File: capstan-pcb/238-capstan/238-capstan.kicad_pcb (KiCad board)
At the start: 2 copper layers, 58 x 67 mm, 53 parts, among them CN1 CN1, IC1 BA6303F, IC2 4013, IC3 BA6411, J1 0, J2 0

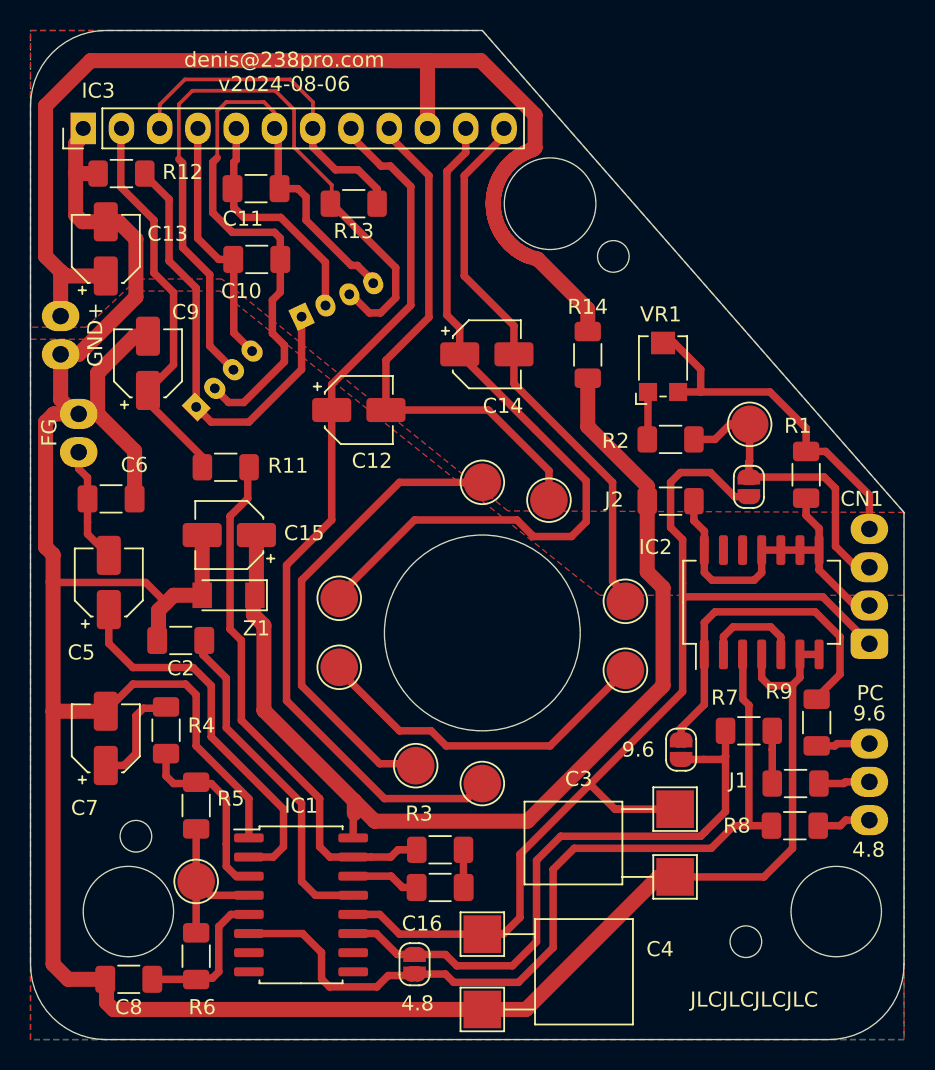
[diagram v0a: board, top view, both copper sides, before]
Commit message: Capstan PCB fix mouting hole position; larger pads for VR1; routing adjustments
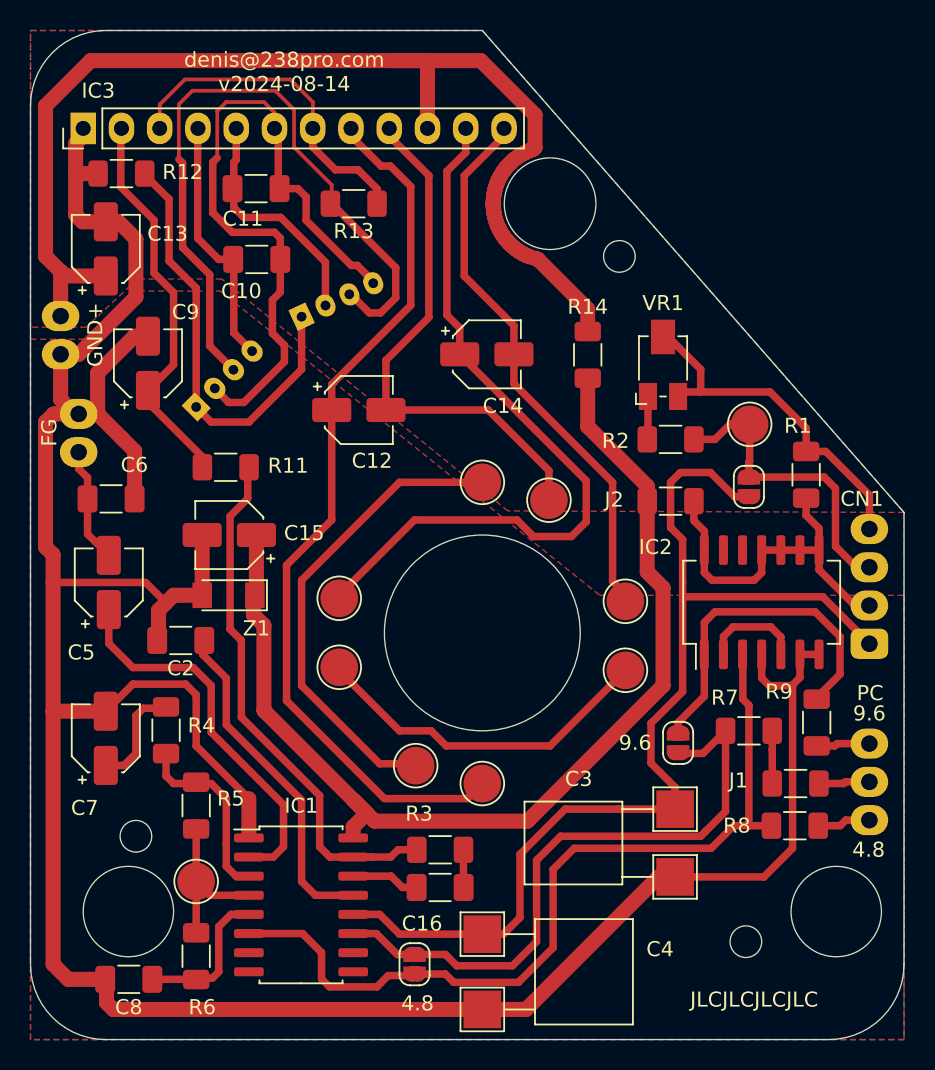
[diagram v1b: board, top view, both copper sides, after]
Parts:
- moved JP2 0.49 mm to (161.0, 97.3)
- moved H2 0.40 mm to (157.1, 65.0)
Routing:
- net Net-(C3-Pad2): track 72.0 -> 71.3 mm
- net Net-(IC1-Pad11): track 41.4 -> 42.0 mm
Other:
- board text added: "denis@238pro.com v2024-08-14"
- board text removed: "denis@238pro.com v2024-08-06"

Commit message: Capstan PCB gerbers v2024-08-15, minor tweaks, sent to fab
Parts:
- moved R11 1.26 mm to (129.7, 79.0)
- moved R14 0.96 mm to (155.0, 72.5)
- moved CN1 0.71 mm to (174.2, 91.2)
- moved IC2 0.70 mm to (165.8, 88.0)
- moved PC1 0.50 mm to (174.2, 97.3)
- moved H2 0.10 mm to (157.0, 65.0)
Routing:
- net +9V: track 70.8 -> 69.6 mm
- net Net-(CN1-Pad3): track 20.4 -> 21.6 mm
- net Net-(CN1-Pad2): track 24.0 -> 25.0 mm
- net Net-(IC2-Pad1): track 22.7 -> 21.7 mm
- net Net-(CN1-Pad4): track 23.4 -> 24.3 mm
- net Net-(C3-Pad2): track 71.3 -> 72.0 mm
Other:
- board text added: "1"
- board text added: "2"
- board text added: "3"
- board text added: "4"
- board text added: "denis@238pro.com v2024-08-15"
- board text removed: "denis@238pro.com v2024-08-14"

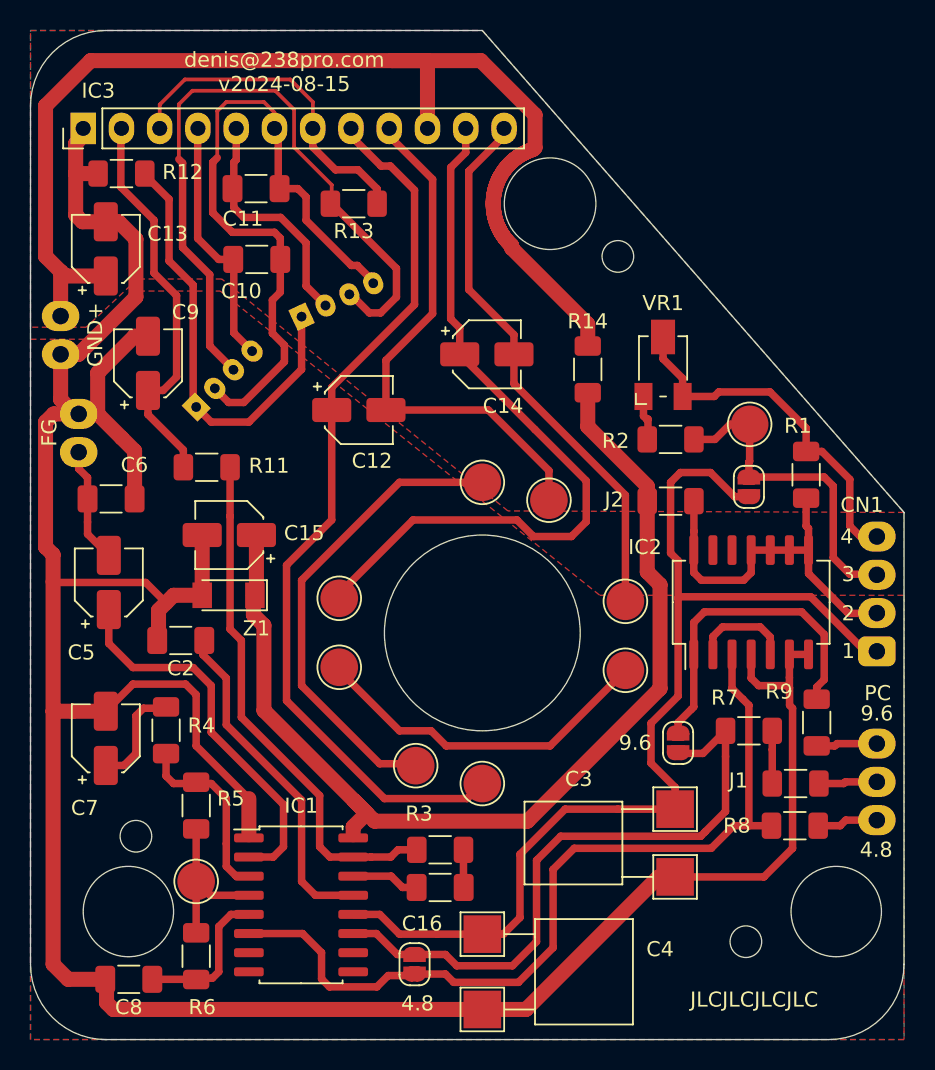
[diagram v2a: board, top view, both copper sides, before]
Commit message: Capstan PCB v2024-09-11, clarified schematic
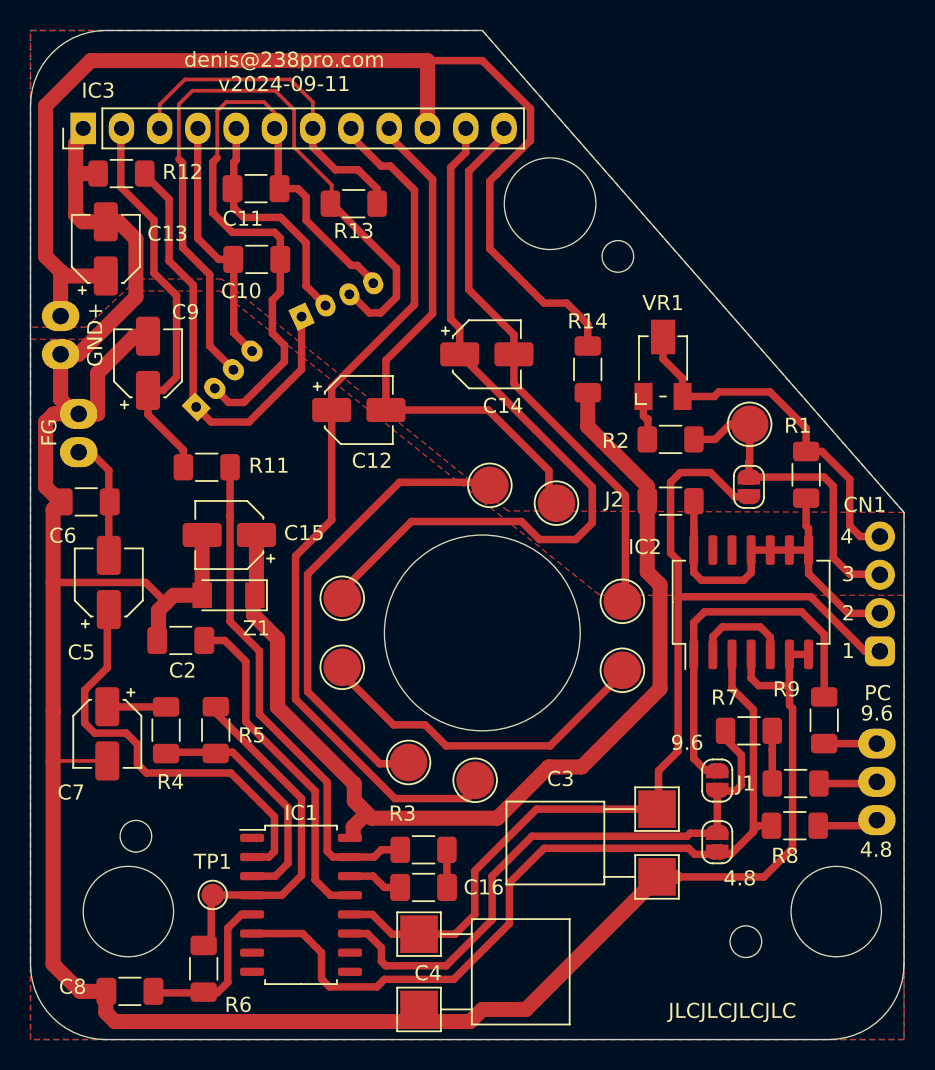
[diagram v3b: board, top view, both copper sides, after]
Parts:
- IC1: footprint Package_SO:SO-16_5.3x10.2mm_P1.27mm -> Package_SO:SOIC-16_4.55x10.3mm_P1.27mm
- TP1: footprint TestPoint:TestPoint_Pad_D2.5mm -> TestPoint:TestPoint_Pad_D1.5mm
- moved JP1 21.7 mm to (163.6, 103.9)
- moved R5 5.18 mm to (130.3, 96.5), turned to 90 degrees
- moved C4 4.20 mm to (143.8, 110.0)
- moved JP2 3.61 mm to (163.6, 99.8)
- moved C6 1.66 mm to (121.7, 81.3), turned to 180 degrees
- moved TP1 1.42 mm to (130.1, 107.4)
- moved C3 1.20 mm to (159.6, 106.2)
- moved C16 1.10 mm to (144.1, 106.9)
- moved R3 1.10 mm to (144.1, 104.4)
- moved R6 0.98 mm to (129.5, 112.3)
- moved C8 0.80 mm to (124.6, 113.8)
- moved W3 0.54 mm to (148.5, 80.2)
- moved W4 0.52 mm to (147.5, 99.8)
- moved R9 0.52 mm to (170.7, 95.8)
- moved C7 0.32 mm to (123.1, 96.7), turned to 270 degrees
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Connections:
- IC1 pad 10: (no net) -> Net-(IC1-Pad10)
- IC1 pad 7: (no net) -> Net-(IC1-Pad7)
- IC1 pad 8: (no net) -> Net-(IC1-Pad8)
- IC1 pad 9: (no net) -> Net-(IC1-Pad9)
- IC2 pad 12: (no net) -> Net-(IC2-Pad12)
- IC2 pad 13: (no net) -> Net-(IC2-Pad13)
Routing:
- net GND: track 193.2 -> 169.9 mm
- net Net-(IC1-Pad4): track 11.0 -> 23.5 mm
- net Net-(IC1-Pad3): track 12.5 -> 16.1 mm
- net Net-(C7-Pad1): track 7.04 -> 3.91 mm
- net Net-(IC2-Pad1): track 21.7 -> 24.7 mm
- net Net-(C3-Pad2): track 72.0 -> 69.3 mm
- net Net-(C5-Pad1): track 25.5 -> 28.1 mm
- net Net-(IC1-Pad11): track 42.0 -> 39.6 mm
- net +12V: track 79.7 -> 78.2 mm
- net Net-(IC1-Pad15): track 34.6 -> 33.4 mm
- net Net-(IC1-Pad6): track 57.0 -> 55.9 mm
- net Net-(C16-Pad2): track 4.52 -> 3.42 mm
- net Net-(C12-Pad1): track 59.7 -> 58.8 mm
- net Net-(C14-Pad1): track 49.4 -> 50.0 mm
- net Net-(C8-Pad1): track 10.0 -> 10.7 mm
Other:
- board text added: "denis@238pro.com v2024-09-11"
- board text removed: "denis@238pro.com v2024-08-15"

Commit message: Capstan PCB gerbers v2024-09-12
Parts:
- moved TP1 13.6 mm to (130.3, 93.8)
- moved C8 6.17 mm to (130.7, 112.9), turned to 270 degrees
- moved R6 5.09 mm to (130.7, 107.3)
- moved C16 2.00 mm to (146.1, 106.9)
- moved C4 2.00 mm to (145.8, 110.0)
- moved IC1 2.00 mm to (138.0, 108.1)
- moved R3 2.00 mm to (146.1, 104.4)
- moved R5 1.50 mm to (130.3, 98.0)
- moved R7 1.00 mm to (165.7, 95.5)
- moved R8 0.65 mm to (169.4, 102.8)
- moved J1 0.60 mm to (169.4, 100.0)
- moved JP2 0.39 mm to (163.3, 100.0)
- moved JP1 0.30 mm to (163.3, 103.9)
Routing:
- net GND: track 169.9 -> 186.4 mm
- net Net-(C8-Pad1): track 10.7 -> 6.44 mm
- net Net-(C3-Pad2): track 69.3 -> 65.6 mm
- net Net-(IC1-Pad11): track 39.6 -> 36.5 mm
- net Net-(IC1-Pad6): track 55.9 -> 53.3 mm
- net +9V: track 69.4 -> 66.9 mm
- net Net-(IC1-Pad4): track 23.5 -> 25.1 mm
- net Net-(C5-Pad1): track 28.1 -> 29.7 mm
- net Net-(IC1-Pad3): track 16.1 -> 17.5 mm
- net Net-(J1-Pad2): track 3.50 -> 4.75 mm
- net Net-(C12-Pad1): track 58.8 -> 57.8 mm
- net Net-(W3-Pad1): track 31.1 -> 30.3 mm
- net Net-(C2-Pad1): track 22.8 -> 23.6 mm
- net Net-(IC1-Pad15): track 33.4 -> 34.2 mm
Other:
- board text added: "denis@238pro.com v2024-09-12"
- board text removed: "denis@238pro.com v2024-09-11"
